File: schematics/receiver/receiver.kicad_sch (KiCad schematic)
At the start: 33 parts, among them M1 Servo, M2 Motor, Q1 2N7000, Q2 2N7000, Q3 2N7000, Q4 2N7000, SW1 SW_Nidec_CAS-120A1, SW2 SW_Push, U1 PIC16F18324-xSL, U2 LM2937xT, U3 NRF24L01_Breakout, U4 L9110H

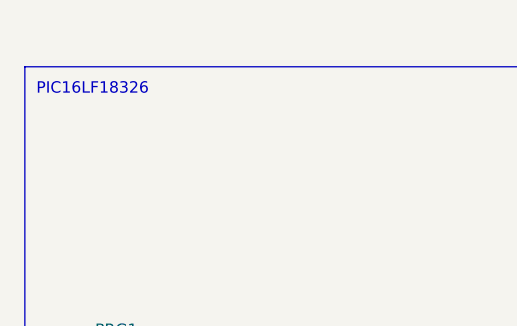
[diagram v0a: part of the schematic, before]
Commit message: Add schematic titles
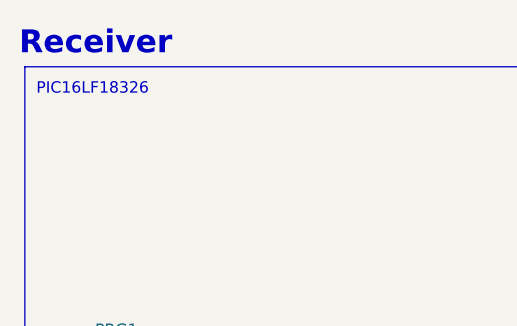
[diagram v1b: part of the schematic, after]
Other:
- note added: "Receiver"
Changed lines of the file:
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@@
+		)
+	)
+	(text "Receiver"
+		(exclude_from_sim no)
+		(at 27.305 38.1 0)
+		(effects
+			(font
+				(size 2.54 2.54)
+				(thickness 0.508)
+				(bold yes)
+			)
+			(justify left)
 		)
 	)

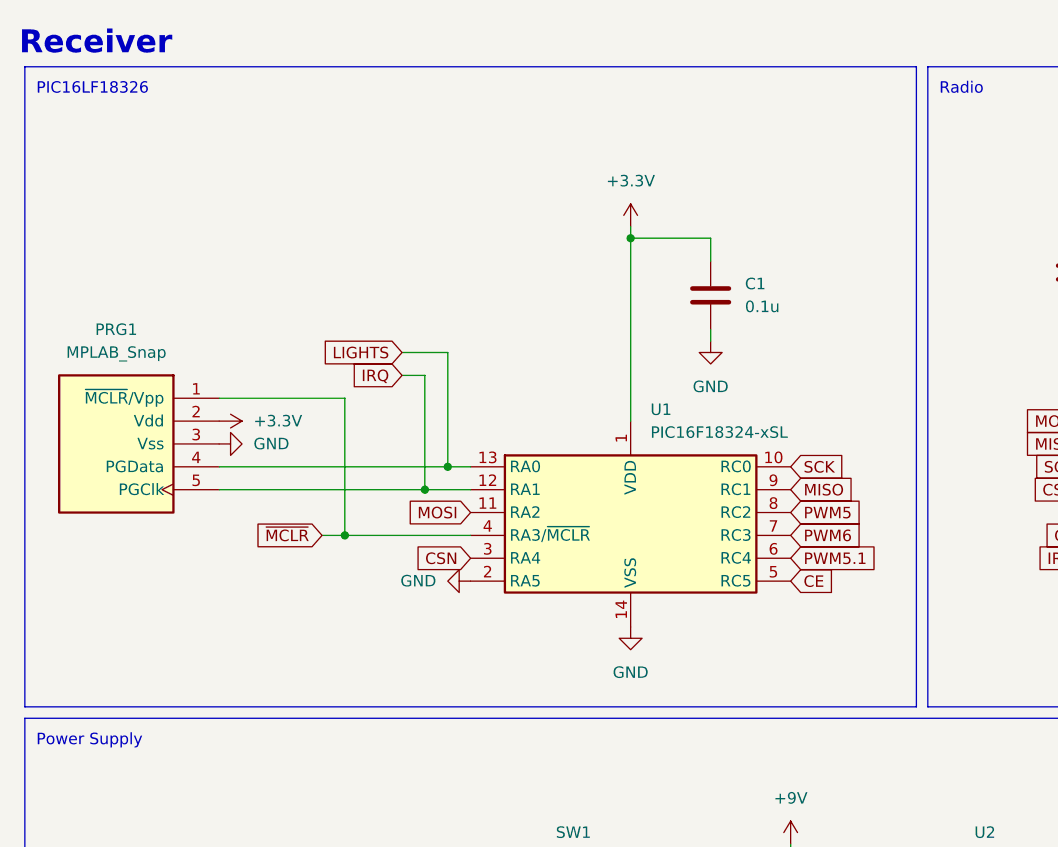
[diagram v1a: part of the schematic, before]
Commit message: Change mcu type select to be pull down for RX board
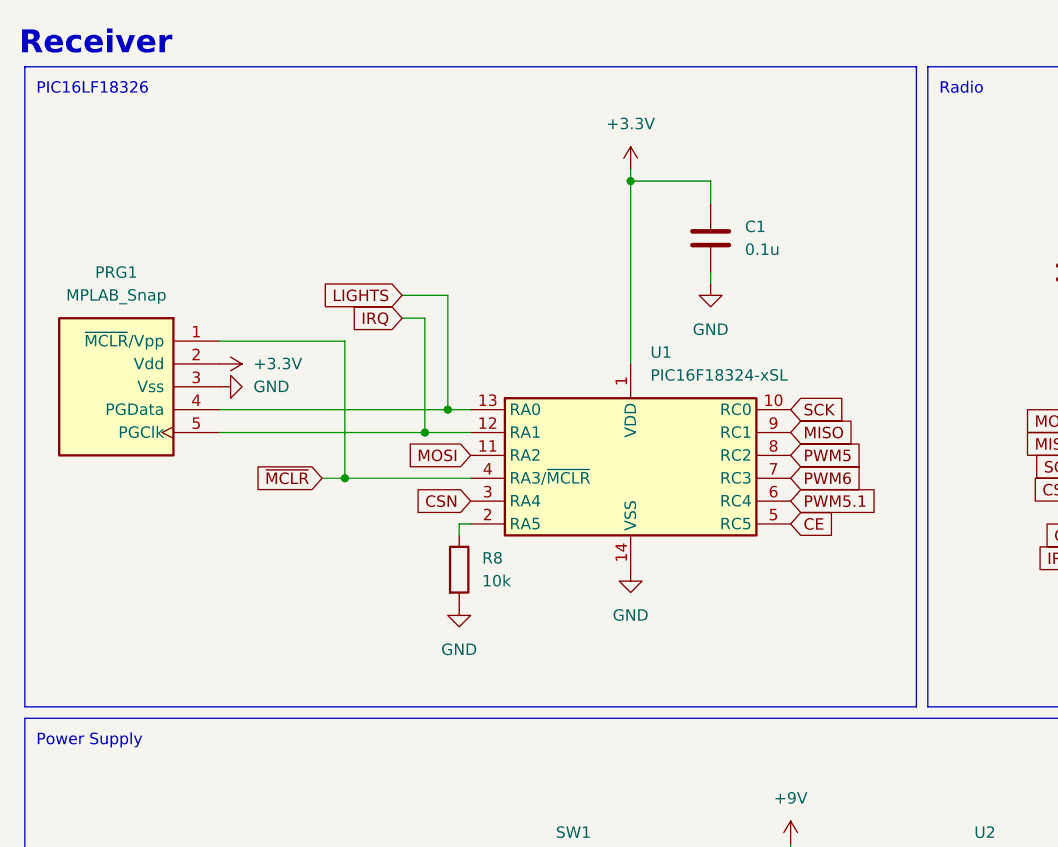
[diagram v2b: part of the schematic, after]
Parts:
- added R8: 10k, Resistor_THT:R_Axial_DIN0204_L3.6mm_D1.6mm_P7.62mm_Horizontal, symbol Device:R
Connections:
- net GND: now also R8.2; no longer U1.2 (RA5)
- new net: R8.1, U1.2 (RA5)
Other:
- moved on the sheet: C1, PRG1, U1

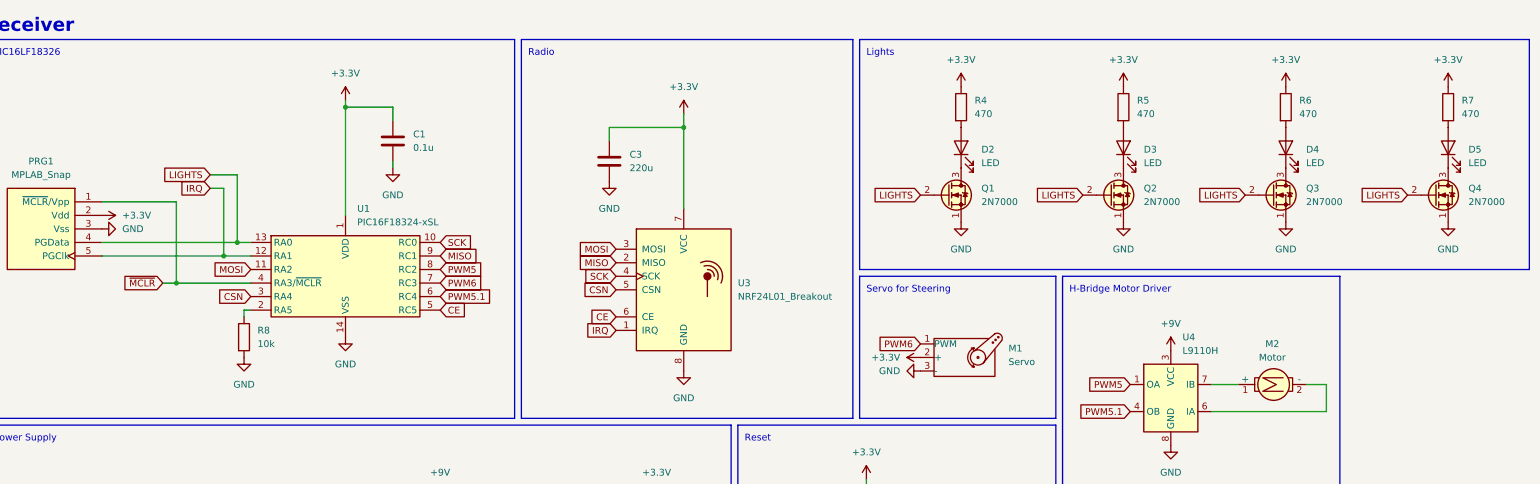
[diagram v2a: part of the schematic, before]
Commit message: Add pull down resistor for LED control on receiver board
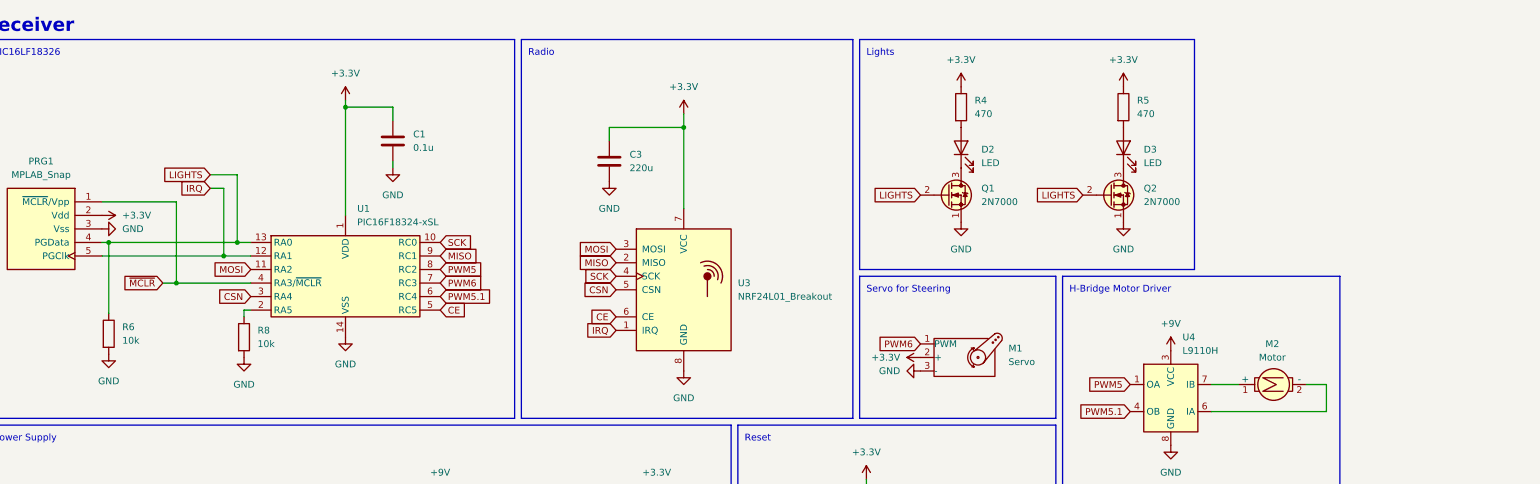
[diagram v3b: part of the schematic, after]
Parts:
- removed D4, D5: LED, LED_THT:LED_D5.0mm, symbol Device:LED
- removed Q3, Q4: 2N7000, Package_TO_SOT_THT:TO-92_Inline_Wide, symbol ME218_BaseLib:2N7000
- removed R7: 470, Resistor_THT:R_Axial_DIN0204_L3.6mm_D1.6mm_P7.62mm_Horizontal, symbol Device:R
- R6: value 470 -> 10k
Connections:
- net +3.3V: no longer R6.1
- net GND: now also R6.2
- net LIGHTS: now also R6.1

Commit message: Remove programing ports and reset btn from final boards
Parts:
- removed C5: 0.1u, Capacitor_THT:CP_Radial_D5.0mm_P2.50mm, symbol Device:C
- removed D1: LED, LED_THT:LED_D5.0mm, symbol Device:LED
- removed PRG1: MPLAB_Snap, Connector_PinSocket_2.54mm:PinSocket_1x05_P2.54mm_Vertical, symbol ME218_BaseLib:MPLAB_Snap
- removed R1: 470, Resistor_THT:R_Axial_DIN0204_L3.6mm_D1.6mm_P7.62mm_Horizontal, symbol Device:R
- removed R2: 1k, Resistor_THT:R_Axial_DIN0204_L3.6mm_D1.6mm_P7.62mm_Horizontal, symbol Device:R
- removed R3: 10k, Resistor_THT:R_Axial_DIN0204_L3.6mm_D1.6mm_P7.62mm_Horizontal, symbol Device:R
- removed SW2: SW_Push, transmitter_footprints:SW_1825910-6-4, symbol Switch:SW_Push
- added H1, H2, H3, H4: MountingHole_Pad, MountingHole:MountingHole_2.5mm_Pad_TopBottom, symbol Mechanical:MountingHole_Pad
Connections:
- net +3.3V: now also U3.2 (VCC); no longer U3.7 (VCC)
- net CE: now also U3.3 (CE); no longer U3.6 (CE)
- net CSN: now also U3.4 (~{CSN}); no longer U3.5 (CSN)
- net GND: now also U3.1 (GND), H1.1, H2.1, H3.1, H4.1; no longer U3.8 (GND)
- net IRQ: now also U3.8 (IRQ); no longer U3.1 (IRQ)
- net MISO: now also U3.7 (MISO); no longer U3.2 (MISO)
- net MOSI: now also U3.6 (MOSI); no longer U3.3 (MOSI)
- net SCK: now also U3.5 (SCK); no longer U3.4 (SCK)
- net ~{MCLR}: no longer names the net of U1.4 (RA3/~{MCLR})
- no-connect marks 0 -> 1
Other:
- note removed: "Reset"

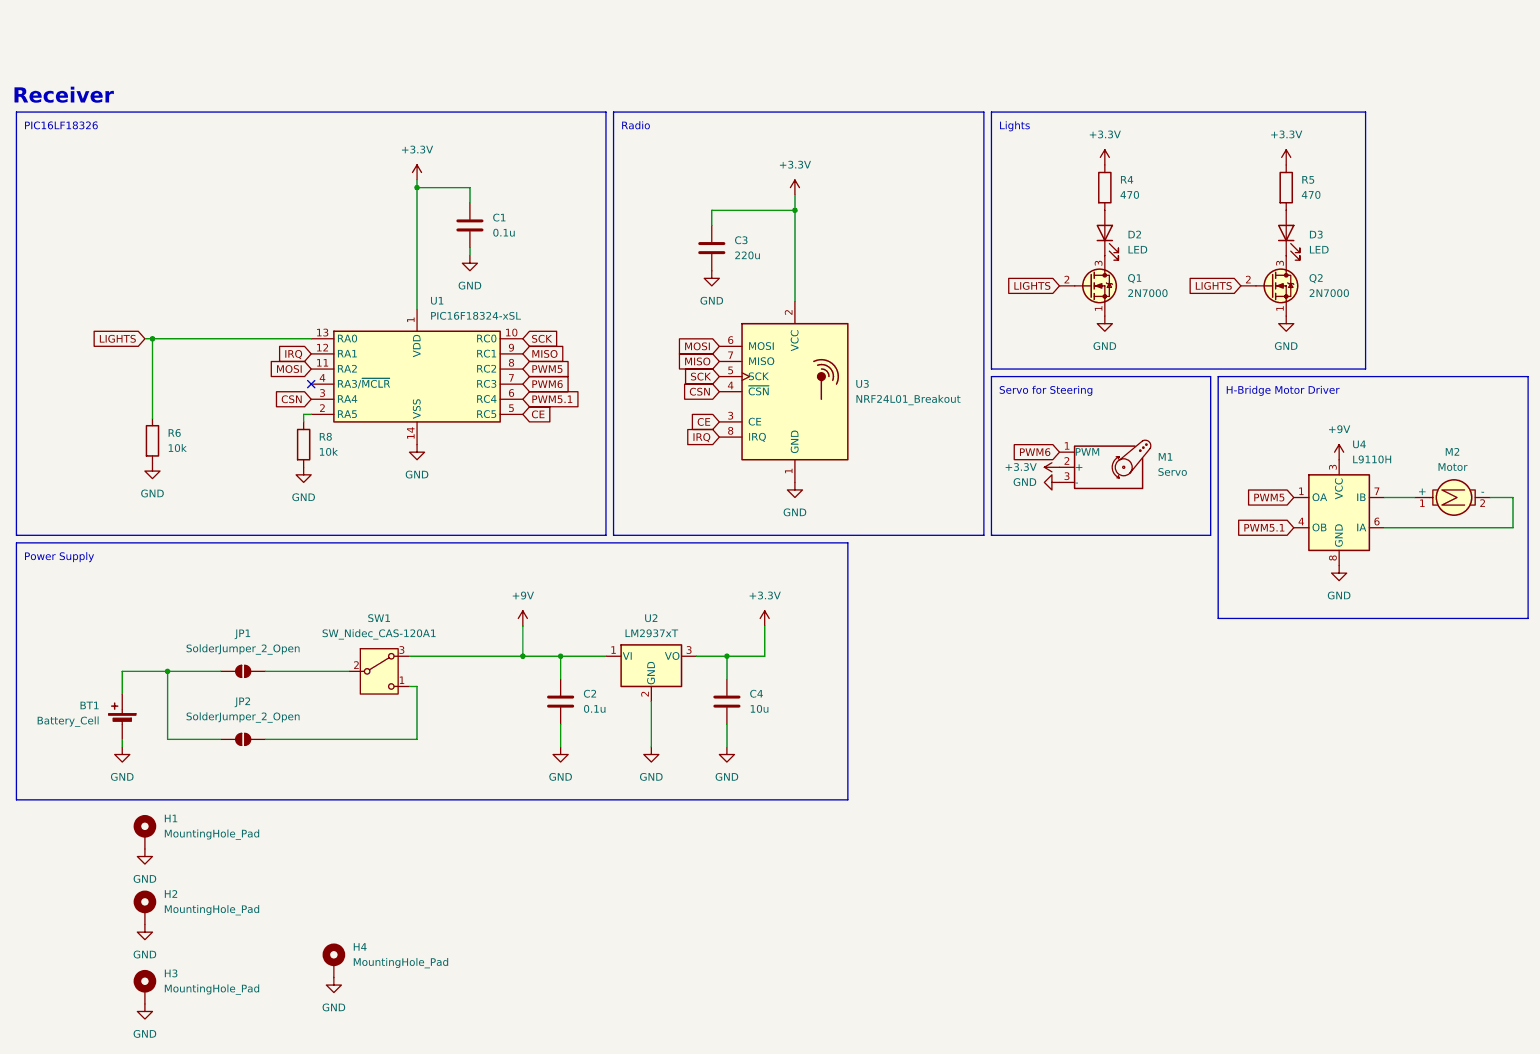
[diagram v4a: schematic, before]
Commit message: Make receiver schematic more readable and add images
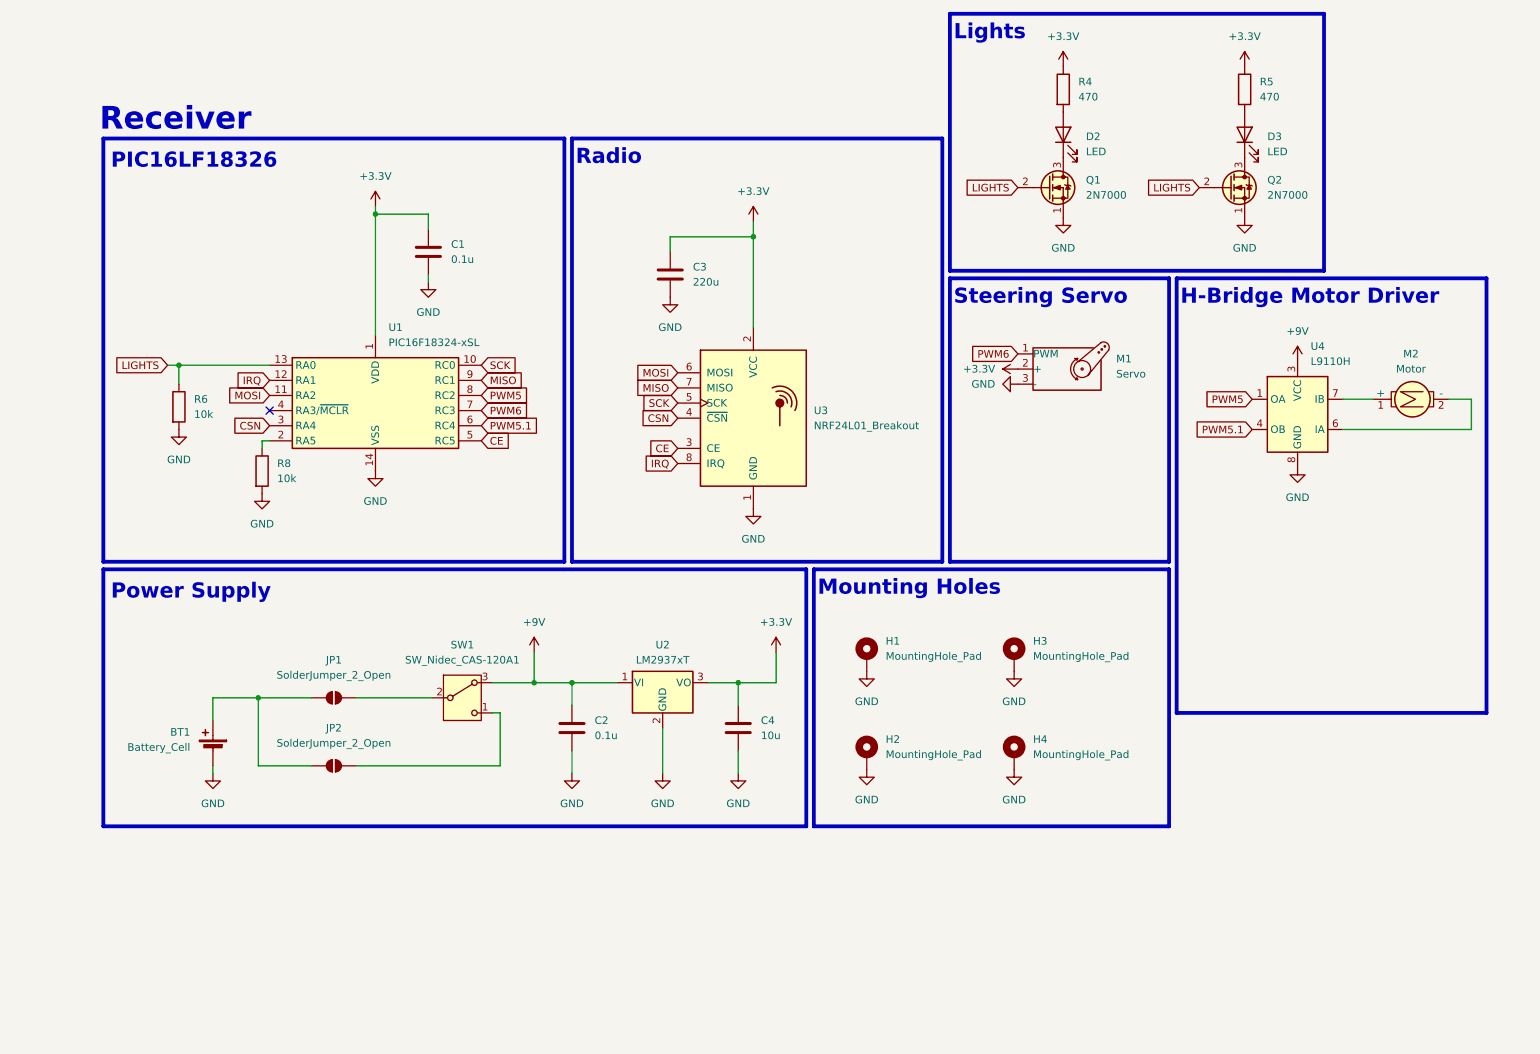
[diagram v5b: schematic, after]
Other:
- note added: "Mounting Holes"
- note added: "Steering Servo"
- note removed: "Servo for Steering"
- moved on the sheet: BT1, C1, C2, C3, C4, D2, D3, H1, H2, H3, H4, JP1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

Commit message: Update BOM for transmitter
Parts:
- C1, C2: Mfn (none) -> Vishay Beyschlag/Draloric/BC Components; Mfn PN (none) -> K104K15X7RF5TL2; Supplier (none) -> DigiKey; Supplier PN (none) -> BC1084TR-ND
- C3: Mfn (none) -> KEMET; Mfn PN (none) -> ESY227M035AH1AA; Supplier (none) -> DigiKey; Supplier PN (none) -> 399-6122-ND
- C4: Mfn (none) -> KEMET; Mfn PN (none) -> ESL106M100AE3AA; Supplier (none) -> DigiKey; Supplier PN (none) -> 399-15738-ND
- D2, D3: Mfn (none) -> Würth Elektronik; Mfn PN (none) -> 151051RS11000; Supplier (none) -> DigiKey; Supplier PN (none) -> 732-5016-ND
- M1: Mfn (none) -> DFRobot; Mfn PN (none) -> SER0006; Supplier (none) -> DigiKey; Supplier PN (none) -> 1738-1385-ND
- M2: Mfn (none) -> Adafruit Industries LLC; Mfn PN (none) -> 711; Supplier (none) -> DigiKey; Supplier PN (none) -> 1528-1150-ND
- Q1, Q2: Mfn (none) -> Diotec Semiconductor; Mfn PN (none) -> 2N7000; Supplier (none) -> DigiKey; Supplier PN (none) -> 4878-2N7000CT-ND
- R4, R5: Mfn (none) -> Stackpole Electronics Inc; Mfn PN (none) -> CF14JT470R; Supplier (none) -> DigiKey; Supplier PN (none) -> CF14JT470RTR-ND
- R6: Mfn (none) -> Stackpole Electronics Inc; Mfn PN (none) -> CF14JT10K0; Supplier (none) -> DigiKey; Supplier PN (none) -> CF14JT10K0TR-ND
- R8: Mfn (none) -> Stackpole Electronics Inc; Mfn PN (none) -> CF14JT10K0; Supplier (none) -> DigiKey
- SW1: Mfn (none) -> E-Switch; Mfn PN (none) -> EG1218; Supplier (none) -> DigiKey; Supplier PN (none) -> EG1903-ND
- U1: Mfn (none) -> Microchip Technology; Mfn PN (none) -> PIC16LF18326-I/P; Supplier (none) -> DigiKey; Supplier PN (none) -> PIC16LF18326-I/P-ND
- U2: Mfn (none) -> Texas Instruments; Mfn PN (none) -> LM2937ET-3.3/NOPB; Supplier (none) -> DigiKey; Supplier PN (none) -> LM2937ET-3.3/NOPB-ND
- U3: Supplier PN (none) -> https://www.aliexpress.us/item/3256809251216534.html?src=go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
- U4: Mfn (none) -> Adafruit Industries LLC; Mfn PN (none) -> 4489; Supplier (none) -> DigiKey; Supplier PN (none) -> 1528-4489-ND
